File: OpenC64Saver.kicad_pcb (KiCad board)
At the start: 2 copper layers, 21 x 46 mm, 17 parts, among them J1 Power I/O, Q1 PN2222A, Q2 PN2222A, X1 OSHW_LOGO, X2 SCREW_HOLE, X3 SCREW_HOLE

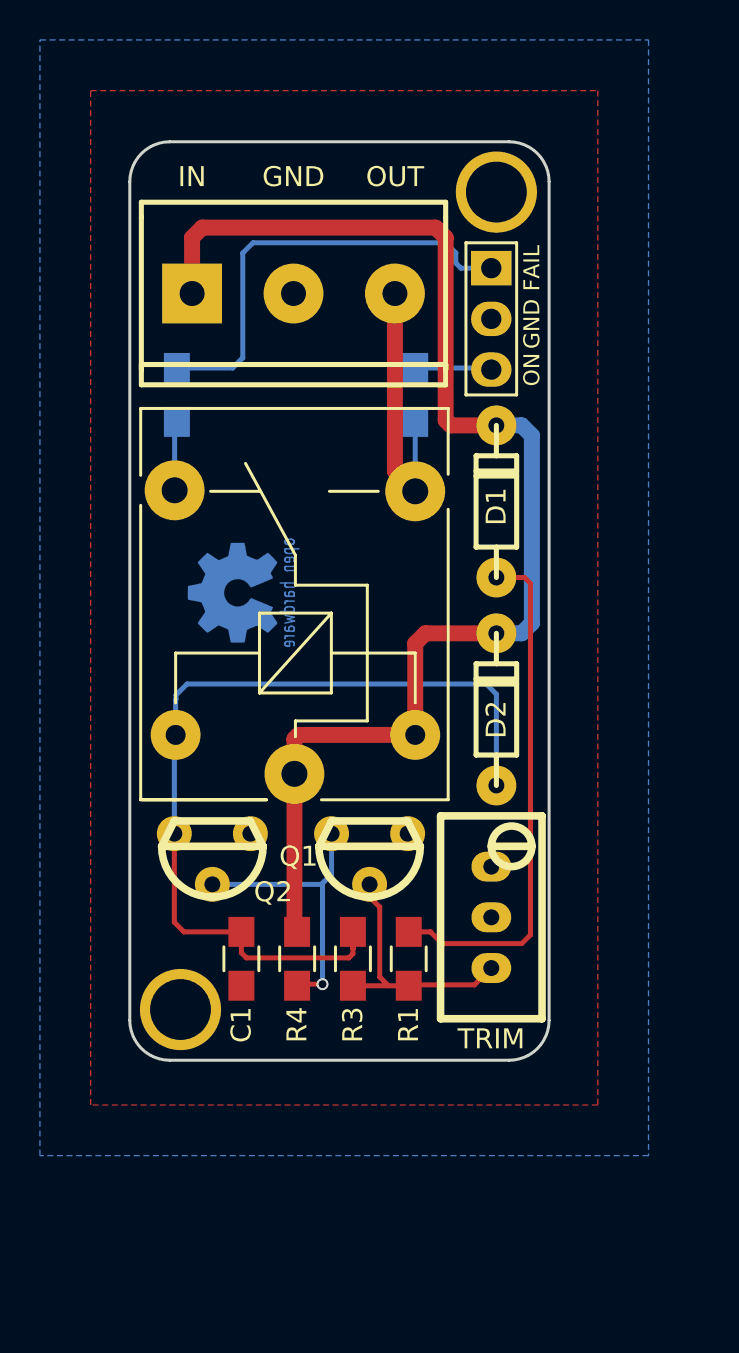
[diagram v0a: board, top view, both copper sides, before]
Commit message: Experimental full through-hole version
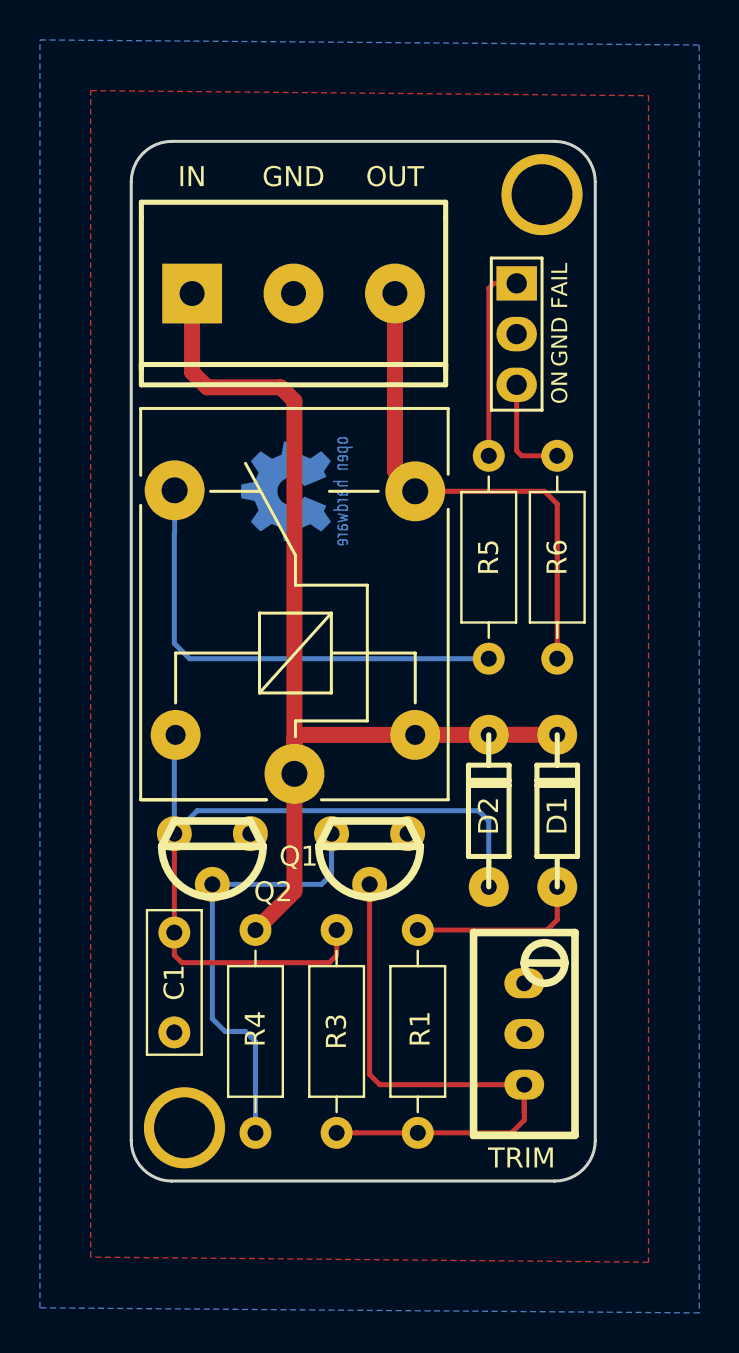
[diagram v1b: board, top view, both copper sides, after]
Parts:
- C1: footprint Resistors_SMD:R_0805_HandSoldering -> Capacitor_THT:C_Disc_D7.0mm_W2.5mm_P5.00mm
- R1, R3, R4: footprint Resistors_SMD:R_0805_HandSoldering -> Resistor_THT:R_Axial_DIN0207_L6.3mm_D2.5mm_P10.16mm_Horizontal
- R5, R6: footprint Resistors_SMD:R_0805_HandSoldering -> Resistor_THT:R_Axial_DIN0207_L6.3mm_D2.5mm_P10.16mm_Horizontal; moved to F.Cu
- moved R5 20.5 mm to (154.6, 99.6)
- moved D1 15.8 mm to (158.0, 107.2)
- moved R6 15.0 mm to (158.0, 99.6)
- moved R2 6.07 mm to (156.3, 118.4)
- moved X3 5.93 mm to (139.3, 123.1)
- moved X1 5.74 mm to (144.4, 91.2)
- moved D2 5.09 mm to (154.6, 107.2)
- moved C1 3.61 mm to (138.8, 113.3)
- moved R4 2.54 mm to (142.9, 113.2)
- moved X2 2.29 mm to (157.2, 76.3)
- moved R3 1.66 mm to (146.9, 113.2)
- moved R1 1.51 mm to (151.0, 113.2)
- moved D3 1.48 mm to (156.0, 80.8)
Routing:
- net Net-(R5-Pad1): track 3.47 -> 23.7 mm
- net Net-(D1-Pad2): track 26.0 -> 8.85 mm
- net Net-(Q1-Pad2): track 12.7 -> 29.4 mm
- net VCC: track 65.8 -> 52.0 mm
- net Net-(D3-Pad1): track 22.2 -> 9.88 mm
- net +5V: track 13.8 -> 25.4 mm
- net Net-(Q1-Pad3): track 14.5 -> 22.1 mm, vias 1 -> 0
- net Net-(C1-Pad1): track 44.1 -> 40.5 mm
- net Net-(D3-Pad3): track 3.84 -> 5.44 mm
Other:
- board size 21 x 46 mm -> 23.2 x 52.1 mm
- net class Default: clearance 0.2 -> 0.15
- net class Power: clearance 0.2 -> 0.15
- rule trace_clearance: 0.2 -> 0.15
- board text added: "V4"
- board text added: "github.com/ SukkoPera/ OpenC64Saver"
- board text removed: "V3"
- board text removed: "github.com/SukkoPera/OpenC64Saver"

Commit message: Minor fix
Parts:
- moved D3 0.38 mm to (156.3, 80.8)
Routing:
- net Net-(C1-Pad1): track 40.5 -> 47.4 mm
- net Net-(D3-Pad1): track 9.88 -> 11.0 mm
